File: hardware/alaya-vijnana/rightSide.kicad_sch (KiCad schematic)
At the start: 0 parts

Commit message: schematics done outside of cluster to main connectors, PCB laid out
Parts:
- added C26: 1uf, Capacitor_SMD:C_0603_1608Metric_Pad1.08x0.95mm_HandSolder, symbol Device:C
- added C27, C28, C29: 100nF, Capacitor_SMD:C_0603_1608Metric_Pad1.08x0.95mm_HandSolder, symbol Device:C
- added C30, C36: 4.7uF, Capacitor_SMD:C_0603_1608Metric_Pad1.08x0.95mm_HandSolder, symbol Device:C
- added C31, C32, C41, C42: 12pF, Capacitor_SMD:C_0603_1608Metric_Pad1.08x0.95mm_HandSolder, symbol Device:C_Small
- added C33, C34: 100pF, Capacitor_SMD:C_0603_1608Metric_Pad1.08x0.95mm_HandSolder, symbol Device:C
- added C35: 820pF, Capacitor_SMD:C_0603_1608Metric_Pad1.08x0.95mm_HandSolder, symbol Device:C
- added C37, C38, C45, C46, C47: 4.7uF, Capacitor_SMD:C_0603_1608Metric_Pad1.08x0.95mm_HandSolder, symbol Device:C_Small
- added C39: 1uF, Capacitor_SMD:C_0603_1608Metric_Pad1.08x0.95mm_HandSolder, symbol Device:C
- added C40: 47nF, Capacitor_SMD:C_0603_1608Metric_Pad1.08x0.95mm_HandSolder, symbol Device:C
- added C43: 10uF, Capacitor_SMD:C_0603_1608Metric_Pad1.08x0.95mm_HandSolder, symbol Device:C_Small
- added C44: 1uF, Capacitor_SMD:C_0603_1608Metric_Pad1.08x0.95mm_HandSolder, symbol Device:C_Small
- added C48: 0.8pF, Capacitor_SMD:C_0603_1608Metric_Pad1.08x0.95mm_HandSolder, symbol Device:C_Small
- added C49: 0.5pF, Capacitor_SMD:C_0603_1608Metric_Pad1.08x0.95mm_HandSolder, symbol Device:C_Small
- added C50: N.C., Capacitor_SMD:C_0603_1608Metric_Pad1.08x0.95mm_HandSolder, symbol Device:C_Small
- added J3: Bat, Connector_JST:JST_PH_S2B-PH-K_1x02_P2.00mm_Horizontal, symbol Connector_Generic:Conn_01x02
- added J4: USB_C_Receptacle_USB2.0_16P, Connector_USB:USB_C_Receptacle_GCT_USB4085, symbol Connector:USB_C_Receptacle_USB2.0_16P
- added L5: 15nH, Inductor_SMD:L_0603_1608Metric, symbol Device:L
- added L6, L7: 10uH, Inductor_SMD:L_0603_1608Metric, symbol Device:L
- added L8: 4.7nH, Inductor_SMD:L_0402_1005Metric_Pad0.77x0.64mm_HandSolder, symbol Device:L
- added LED2: Charge_LED, PCM_LED_SMD_AKL:LED_1206_3216Metric, symbol PCM_LED_AKL:LED_1206_Orange
- added R10: 10M, Resistor_SMD:R_0603_1608Metric_Pad0.98x0.95mm_HandSolder, symbol Device:R
- added R11, R12, R9: 10k, Resistor_SMD:R_0603_1608Metric_Pad0.98x0.95mm_HandSolder, symbol Device:R_Small
- added R13, R14: 5.1k, Resistor_SMD:R_0603_1608Metric_Pad0.98x0.95mm_HandSolder, symbol Device:R
- added R8: 2k, Resistor_SMD:R_0603_1608Metric_Pad0.98x0.95mm_HandSolder, symbol Device:R_Small
- added SW23: Power_Switch, Button_Switch_THT:SW_E-Switch_EG1224_SPDT_Angled, symbol Switch:SW_Wuerth_450301014042
- added TP2: Charge Boost, Resistor_SMD:R_2816_7142Metric_Pad3.20x4.45mm_HandSolder, symbol Connector:TestPoint_2Pole
- added U4: nRF52840, Package_DFN_QFN:Nordic_AQFN-73-1EP_7x7mm_P0.5mm, symbol MCU_Nordic:nRF52840
- added U5: XC6220B331MR, Package_TO_SOT_SMD:SOT-23-5, symbol Regulator_Linear:XC6220B331MR
- added U6: BQ24075RGT, Package_DFN_QFN:VQFN-16-1EP_3x3mm_P0.5mm_EP1.6x1.6mm, symbol Battery_Management:BQ24075RGT
- added X2: 32.768kHz, Crystal:Crystal_SMD_2012-2Pin_2.0x1.2mm, symbol PCM_Crystal_AKL:Crystal_Generic
- added Y2: 32Mhz, Crystal:Crystal_SMD_3225-4Pin_3.2x2.5mm_HandSoldering, symbol Device:Crystal_GND2
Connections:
- new net: L5.2, L6.1
- new net: L6.2, U4.B3 (DCC)
- new net: R11.1, U6.1 (TS)
- new net: R9.1, TP2.1, U6.16 (ISET)
- new net: C42.2, U4.F2 (XL2/P0.01), X2.1
- new net: C41.2, U4.D2 (XL1/P0.00), X2.2
- new net: C35.2, U4.N24 (DEC5)
- new net: J4.A5 (CC1), R13.1
- new net: J4.B5 (CC2), R14.1
- new net: C32.1, U4.A23 (XC2), Y2.3
- new net: L7.1, U4.AB2 (DCCH)
- new net: C36.2, U4.AC5 (DECUSB)
- new net: C31.1, U4.B24 (XC1), Y2.1
- new net: C39.1, C40.1, L5.1, U4.B5 (DEC4), U4.E24 (DEC6)
- new net: C33.2, U4.C1 (DEC1)
- new net: C34.2, U4.D23 (DEC3)
- new net: LED2.1 (K), U6.9 (~{CHG})
- new net: LED2.2 (A), R12.1
- new net: R8.2, TP2.2
- new net ANT: C48.1, L8.1, U4.H23 (ANT)
- new net BAT+: J3.1 (Pin_1), SW23.1 (B)
- new net BAT-: J3.2 (Pin_2)
- new net D+: J4.A6 (D+), J4.B6 (D+), U4.AD6 (D+)
- new net D-: J4.A7 (D-), J4.B7 (D-), U4.AD4 (D-)
- new net EXT_VCC: C45.1, U5.5 (VOUT)
- new net GND: C26.2, C27.2, C28.2, C29.2, C30.2, C31.2, C32.2, C33.1, C34.1, C35.1, C36.1, C37.1, C38.2, C39.2, C40.2, C41.1, C42.1, C43.2, C44.1, C45.2, C47.2, C48.2, C49.2, C50.2, J4.A1 (GND), J4.A12 (GND), J4.B1 (GND), J4.B12 (GND), R11.2, R13.2, R14.2, R8.1, R9.2, U4.B7 (VSS), U4.EP (VSS), U4.F23 (VSS_PA), U5.2 (GND), U6.15 (SYSOFF), U6.17 (VSS), U6.4 (~{CE}), U6.5 (EN2), U6.8 (VSS), Y2.2
- new net POWER_PIN: R10.2, U4.AD8 (P0.13), U5.3 (CE)
- new net RF: C49.1, C50.1, L8.2
- new net VBAT: C47.1, SW23.3 (A), U6.2 (BAT), U6.3 (BAT)
- new net VBUS: C38.1, C44.2, J4.A4 (VBUS), J4.A9 (VBUS), J4.B4 (VBUS), J4.B9 (VBUS), U4.AD2 (VBUS), U6.13 (IN)
- new net VDDH: C37.2, C43.1, C46.2, R10.1, R12.2, U4.Y2 (VDDH), U5.1 (VIN), U6.10 (OUT), U6.11 (OUT), U6.6 (EN1)
- new net VDD_NRF: C26.1, C27.1, C28.1, C29.1, C30.1, L7.2, U4.A22 (VDD), U4.AD14 (VDD), U4.AD23 (VDD), U4.B1 (VDD), U4.W1 (VDD)
- no-connect marks 0 -> 8
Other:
- added sheet Right Key Matrix (rightMatrix.kicad_sch)
- note added: "Battery Connector"
- note added: "Charger"
- note added: "Power Switch"
- note added: "RF Circutry"
- note added: "VCC Regulator & Cutoff"
- note added: "nRF52840"

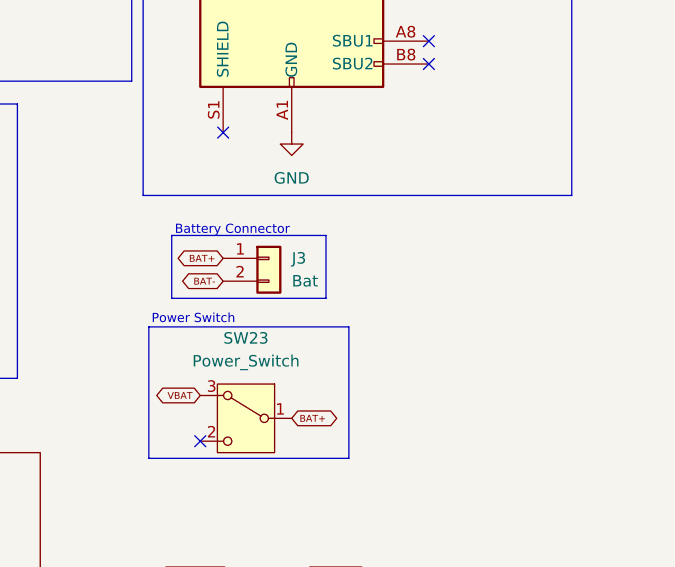
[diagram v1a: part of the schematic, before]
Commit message: left side wired up
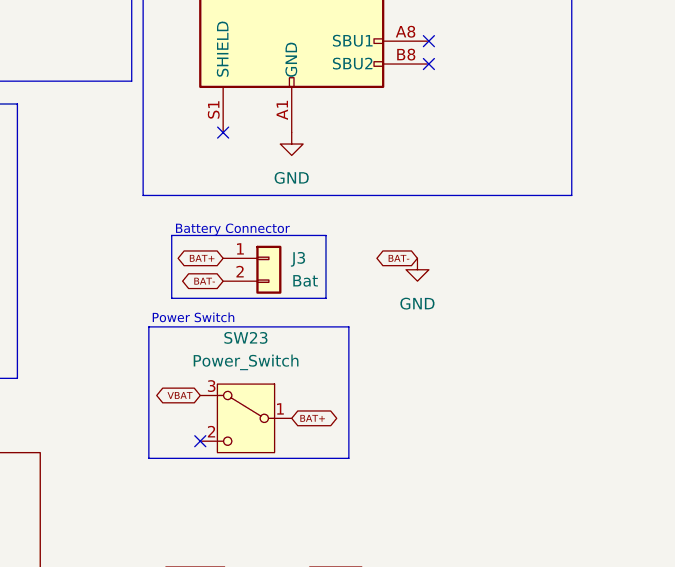
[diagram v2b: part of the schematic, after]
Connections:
- net BAT- is gone; now on net GND: J3.2 (Pin_2)
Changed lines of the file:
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@@
 		)
 	)
+	(global_label "BAT-"
+		(shape bidirectional)
+		(at 256.54 97.79 180)
+		(fields_autoplaced yes)
+		(effects
+			(font
+				(size 0.762 0.762)
+			)
+			(justify right)
+		)
+		(property "Intersheetrefs" "${INTERSHEET_REFS}"
+			(at 251.1427 97.79 0)
+			(effects
+				(font
+					(size 1.27 1.27)
+				)
+				(justify right)
+				(hide yes)
+			)
+		)
+	)
 	(global_label "ANT"
 		(shape bidirectional)
@@
 					(unit 1)
 				)
+			)
+		)
+	)
+	(symbol
+		(lib_id "power:GND")
+		(at 256.54 97.79 0)
+		(unit 1)
+		(exclude_from_sim no)
+		(in_bom yes)
+		(on_board yes)
+		(dnp no)
+		(fields_autoplaced yes)
+		(property "Reference" "#PWR053"
+			(at 256.54 104.14 0)
+			(effects
+				(font
+					(size 1.27 1.27)
+				)
+				(hide yes)
+			)
+		)
+		(property "Value" "GND"
+			(at 256.54 102.87 0)
+			(effects
+				(font
+					(size 1.27 1.27)
+				)
+			)
+		)
+		(property "Footprint" ""
+			(at 256.54 97.79 0)
+			(effects
+				(font
+					(size 1.27 1.27)
+				)
+				(hide yes)
+			)
+		)
+		(property "Datasheet" ""
+			(at 256.54 97.79 0)
+			(effects
+				(font
+					(size 1.27 1.27)
+				)
+				(hide yes)
+			)
+		)
+		(property "Description" "Power symbol creates a global label with name \"GND\" , ground"
+			(at 256.54 97.79 0)
+			(effects
+				(font
+					(size 1.27 1.27)
+				)
+				(hide yes)
+			)
+		)
+		(pin "1"
+		)
+		(instances
+			(project "alaya-vijnana"
+				(path "/a3984b5f-5482-487c-827c-93986b80e1c8/13abaaa7-652e-4a16-9fc7-1610d4c7b512"
+					(reference "#PWR053")
+					(unit 1)
+				)

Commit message: finished
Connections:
- net COL0: now also U4.R24 (P1.06)
- net COL1: now also U4.U24 (P1.04)
- net COL2: now also U4.W24 (P1.02)
- net COL3: now also U4.Y23 (P1.01)
- net COL4: now also U4.AC21 (P0.25)
- net COL5: now also U4.AD22 (TRACEDATA0/P1.00)
- net COL6: now also U4.AD20 (P0.24)
- net GND: now also C46.1
- net ROW0: now also U4.AD12 (P0.17)
- net ROW1: now also U4.AD16 (P0.20)
- net ROW2: now also U4.AD18 (P0.22)
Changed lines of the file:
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@@
 	(wire
 		(pts
+			(xy 205.74 31.75) (xy 205.74 24.13)
+		)
+		(stroke
+			(width 0)
+			(type default)
+		)
+	)
+	(wire
+		(pts
 			(xy 19.05 121.92) (xy 16.51 121.92)
 		)
@@
 	(wire
 		(pts
+			(xy 212.09 24.13) (xy 212.09 25.4)
+		)
+		(stroke
+			(width 0)
+			(type default)
+		)
+	)
+	(wire
+		(pts
 			(xy 200.66 81.28) (xy 204.47 81.28)
 		)
@@
 	(wire
 		(pts
+			(xy 205.74 24.13) (xy 212.09 24.13)
+		)
+		(stroke
+			(width 0)
+			(type default)
+		)
+	)
+	(wire
+		(pts
 			(xy 39.37 40.64) (xy 39.37 41.91)
 		)
@@
 	(global_label "COL0"
 		(shape bidirectional)
-		(at 251.46 133.35 180)
+		(at 105.41 149.86 0)
 		(fields_autoplaced yes)
 		(effects
@@
 				(size 1.27 1.27)
 			)
-			(justify right)
+			(justify left)
 		)
 		(property "Intersheetrefs" "${INTERSHEET_REFS}"
-			(at 242.5254 133.35 0)
+			(at 114.3446 149.86 0)
 			(effects
 				(font
 					(size 1.27 1.27)
 				)
-				(justify right)
+				(justify left)
 				(hide yes)
 			)
@@
 	(global_label "COL6"
 		(shape bidirectional)
-		(at 251.46 148.59 180)
+		(at 105.41 111.76 0)
 		(fields_autoplaced yes)
 		(effects
@@
 				(size 1.27 1.27)
 			)
-			(justify right)
+			(justify left)
 		)
 		(property "Intersheetrefs" "${INTERSHEET_REFS}"
-			(at 242.5254 148.59 0)
+			(at 114.3446 111.76 0)
 			(effects
 				(font
 					(size 1.27 1.27)
 				)
-				(justify right)
+				(justify left)
 				(hide yes)
 			)
@@
 	(global_label "COL2"
 		(shape bidirectional)
-		(at 251.46 138.43 180)
+		(at 105.41 139.7 0)
 		(fields_autoplaced yes)
 		(effects
@@
 				(size 1.27 1.27)
 			)
-			(justify right)
+			(justify left)
 		)
 		(property "Intersheetrefs" "${INTERSHEET_REFS}"
-			(at 242.5254 138.43 0)
+			(at 114.3446 139.7 0)
 			(effects
 				(font
 					(size 1.27 1.27)
 				)
-				(justify right)
+				(justify left)
 				(hide yes)
 			)
@@
 	(global_label "COL1"
 		(shape bidirectional)
-		(at 251.46 135.89 180)
+		(at 105.41 144.78 0)
 		(fields_autoplaced yes)
 		(effects
@@
 				(size 1.27 1.27)
 			)
-			(justify right)
+			(justify left)
 		)
 		(property "Intersheetrefs" "${INTERSHEET_REFS}"
-			(at 242.5254 135.89 0)
+			(at 114.3446 144.78 0)
 			(effects
 				(font
 					(size 1.27 1.27)
 				)
-				(justify right)
+				(justify left)
 				(hide yes)
 			)
@@
 	(global_label "COL5"
 		(shape bidirectional)
-		(at 251.46 146.05 180)
+		(at 105.41 134.62 0)
 		(fields_autoplaced yes)
 		(effects
@@
 				(size 1.27 1.27)
 			)
-			(justify right)
+			(justify left)
 		)
 		(property "Intersheetrefs" "${INTERSHEET_REFS}"
-			(at 242.5254 146.05 0)
+			(at 114.3446 134.62 0)
 			(effects
 				(font
 					(size 1.27 1.27)
 				)
-				(justify right)
+				(justify left)
 				(hide yes)
 			)
@@
 	(global_label "COL4"
 		(shape bidirectional)
-		(at 251.46 143.51 180)
+		(at 105.41 114.3 0)
 		(fields_autoplaced yes)
 		(effects
@@
 				(size 1.27 1.27)
 			)
-			(justify right)
+			(justify left)
 		)
 		(property "Intersheetrefs" "${INTERSHEET_REFS}"
-			(at 242.5254 143.51 0)
+			(at 114.3446 114.3 0)
 			(effects
 				(font
 					(size 1.27 1.27)
 				)
-				(justify right)
+				(justify left)
 				(hide yes)
 			)
@@
 	(global_label "ROW2"
 		(shape bidirectional)
-		(at 236.22 138.43 180)
+		(at 105.41 106.68 0)
 		(fields_autoplaced yes)
 		(effects
@@
 				(size 1.27 1.27)
 			)
-			(justify right)
+			(justify left)
 		)
 		(property "Intersheetrefs" "${INTERSHEET_REFS}"
-			(at 226.8621 138.43 0)
+			(at 114.7679 106.68 0)
 			(effects
 				(font
 					(size 1.27 1.27)
 				)
-				(justify right)
+				(justify left)
 				(hide yes)
 			)
@@
 	(global_label "ROW0"
 		(shape bidirectional)
-		(at 236.22 133.35 180)
+		(at 105.41 96.52 0)
 		(fields_autoplaced yes)
 		(effects
@@
 				(size 1.27 1.27)
 			)
-			(justify right)
+			(justify left)
 		)
 		(property "Intersheetrefs" "${INTERSHEET_REFS}"
-			(at 226.8621 133.35 0)
+			(at 114.7679 96.52 0)
 			(effects
 				(font
 					(size 1.27 1.27)
 				)
-				(justify right)
+				(justify left)
 				(hide yes)
 			)
@@
 	(global_label "ROW1"
 		(shape bidirectional)
-		(at 236.22 135.89 180)
+		(at 105.41 101.6 0)
 		(fields_autoplaced yes)
 		(effects
@@
 				(size 1.27 1.27)
 			)
-			(justify right)
+			(justify left)
 		)
 		(property "Intersheetrefs" "${INTERSHEET_REFS}"
-			(at 226.8621 135.89 0)
+			(at 114.7679 101.6 0)
 			(effects
 				(font
 					(size 1.27 1.27)
 				)
-				(justify right)
+				(justify left)
 				(hide yes)
 			)
@@
 	(global_label "COL3"
 		(shape bidirectional)
-		(at 251.46 140.97 180)
+		(at 105.41 137.16 0)
 		(fields_autoplaced yes)
 		(effects
@@
 				(size 1.27 1.27)
 			)
-			(justify right)
+			(justify left)
 		)
 		(property "Intersheetrefs" "${INTERSHEET_REFS}"
-			(at 242.5254 140.97 0)
+			(at 114.3446 137.16 0)
 			(effects
 				(font
 					(size 1.27 1.27)
 				)
-				(justify right)
+				(justify left)
 				(hide yes)
 			)
@@
 					(unit 1)
 				)
+			)
+		)
+	)
+	(symbol
+		(lib_id "power:GND")
+		(at 212.09 25.4 0)
+		(unit 1)
+		(exclude_from_sim no)
+		(in_bom yes)
+		(on_board yes)
+		(dnp no)
+		(fields_autoplaced yes)
+		(property "Reference" "#PWR054"
+			(at 212.09 31.75 0)
+			(effects
+				(font
+					(size 1.27 1.27)
+				)
+				(hide yes)
+			)
+		)
+		(property "Value" "GND"
+			(at 212.09 30.48 0)
+			(effects
+				(font
+					(size 1.27 1.27)
+				)
+			)
+		)
+		(property "Footprint" ""
+			(at 212.09 25.4 0)
+			(effects
+				(font
+					(size 1.27 1.27)
+				)
+				(hide yes)
+			)
+		)
+		(property "Datasheet" ""
+			(at 212.09 25.4 0)
+			(effects
+				(font
+					(size 1.27 1.27)
+				)
+				(hide yes)
+			)
+		)
+		(property "Description" "Power symbol creates a global label with name \"GND\" , ground"
+			(at 212.09 25.4 0)
+			(effects
+				(font
+					(size 1.27 1.27)
+				)
+				(hide yes)
+			)
+		)
+		(pin "1"
+		)
+		(instances
+			(project ""
+				(path "/a3984b5f-5482-487c-827c-93986b80e1c8/13abaaa7-652e-4a16-9fc7-1610d4c7b512"
+					(reference "#PWR054")
+					(unit 1)
+				)

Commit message: production stuff
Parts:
- added SW46: SW_Push, Button_Switch_SMD:SW_Push_1P1T_NO_CK_KMR2, symbol Switch:SW_Push
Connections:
- net GND: now also SW46.1
- net at U4.AC13 (P0.18/~{RESET}): now also SW46.2
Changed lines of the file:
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@@
+	)
+	(symbol
+		(lib_id "power:GND")
+		(at 29.21 160.02 0)
+		(unit 1)
+		(exclude_from_sim no)
+		(in_bom yes)
+		(on_board yes)
+		(dnp no)
+		(fields_autoplaced yes)
+		(property "Reference" "#PWR056"
+			(at 29.21 166.37 0)
+			(effects
+				(font
+					(size 1.27 1.27)
+				)
+				(hide yes)
+			)
+		)
+		(property "Value" "GND"
+			(at 29.21 165.1 0)
+			(effects
+				(font
+					(size 1.27 1.27)
+				)
+			)
+		)
+		(property "Footprint" ""
+			(at 29.21 160.02 0)
+			(effects
+				(font
+					(size 1.27 1.27)
+				)
+				(hide yes)
+			)
+		)
+		(property "Datasheet" ""
+			(at 29.21 160.02 0)
+			(effects
+				(font
+					(size 1.27 1.27)
+				)
+				(hide yes)
+			)
+		)
+		(property "Description" "Power symbol creates a global label with name \"GND\" , ground"
+			(at 29.21 160.02 0)
+			(effects
+				(font
+					(size 1.27 1.27)
+				)
+				(hide yes)
+			)
+		)
+		(pin "1"
+		)
+		(instances
+			(project "alaya-vijnana"
+				(path "/a3984b5f-5482-487c-827c-93986b80e1c8/13abaaa7-652e-4a16-9fc7-1610d4c7b512"
+					(reference "#PWR056")
+					(unit 1)
+				)
+			)
+		)
 	)
 	(symbol
@@
 					(unit 1)
 				)
+			)
+		)
+	)
+	(symbol
+		(lib_id "Switch:SW_Push")
+		(at 34.29 160.02 0)
+		(unit 1)
+		(exclude_from_sim no)
+		(in_bom yes)
+		(on_board yes)
+		(dnp no)
+		(fields_autoplaced yes)
+		(property "Reference" "SW46"
+			(at 34.29 152.4 0)
+			(effects
+				(font
+					(size 1.27 1.27)
+				)
+			)
+		)
+		(property "Value" "SW_Push"
+			(at 34.29 154.94 0)
+			(effects
+				(font
+					(size 1.27 1.27)
+				)
+			)
+		)
+		(property "Footprint" "Button_Switch_SMD:SW_Push_1P1T_NO_CK_KMR2"
+			(at 34.29 154.94 0)
+			(effects
+				(font
+					(size 1.27 1.27)
+				)
+				(hide yes)
+			)
+		)
+		(property "Datasheet" "~"
+			(at 34.29 154.94 0)
+			(effects
+				(font
+					(size 1.27 1.27)
+				)
+				(hide yes)
+			)
+		)
+		(property "Description" "Push button switch, generic, two pins"
+			(at 34.29 160.02 0)
+			(effects
+				(font
+					(size 1.27 1.27)
+				)
+				(hide yes)
+			)
+		)
+		(pin "2"
+		)
+		(pin "1"
+		)
+		(instances
+			(project "alaya-vijnana"
+				(path "/a3984b5f-5482-487c-827c-93986b80e1c8/13abaaa7-652e-4a16-9fc7-1610d4c7b512"
+					(reference "SW46")
+					(unit 1)
+				)
